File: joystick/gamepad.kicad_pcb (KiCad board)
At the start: 2 copper layers, 112 x 47.6 mm, 40 parts, among them IC1 ATTINY45-S, P2 CONN_01X04, SW1 SW_PUSH, SW2 SW_PUSH, SW3 SW_PUSH, SW4 SW_PUSH, SW5 SW_PUSH, SW6 SW_PUSH, U1 74LS165, U2 74164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

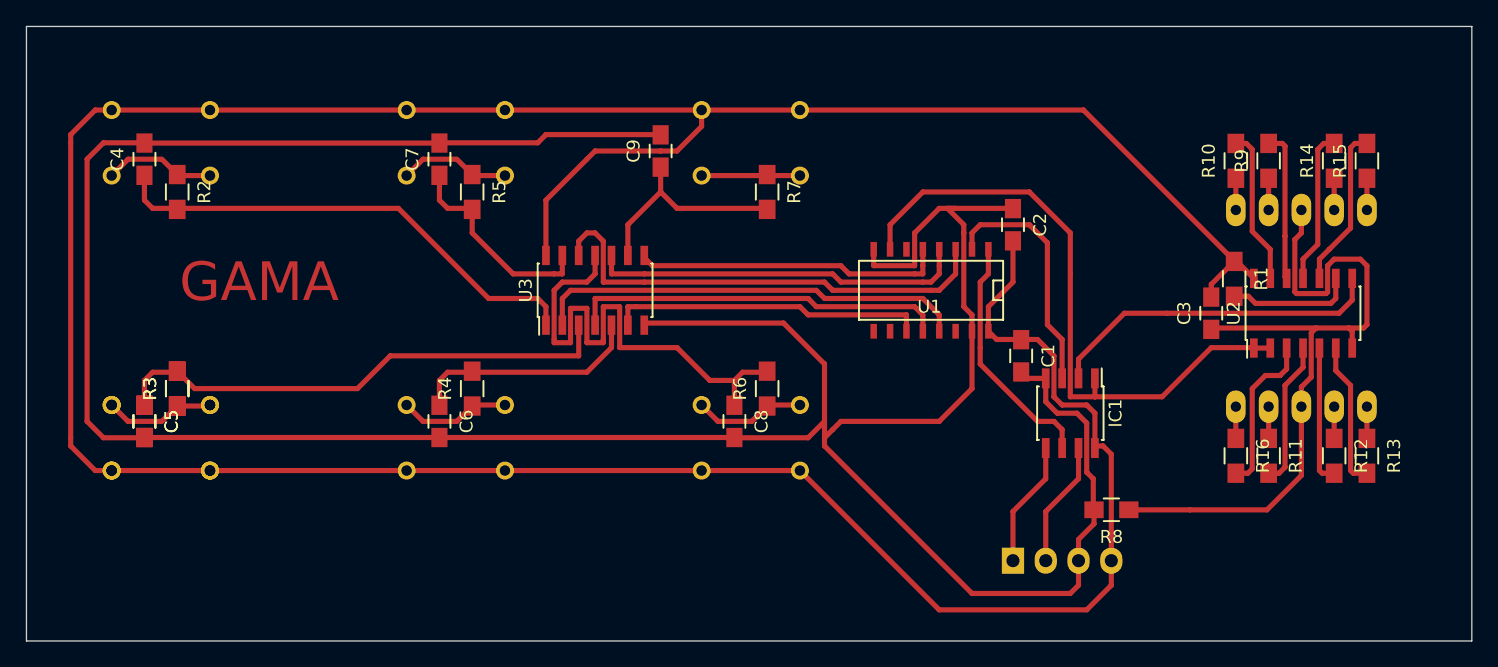
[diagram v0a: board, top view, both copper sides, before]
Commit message: Fixed hardware bug (74LS14 inputs were left floating) Changed schematics accordingly
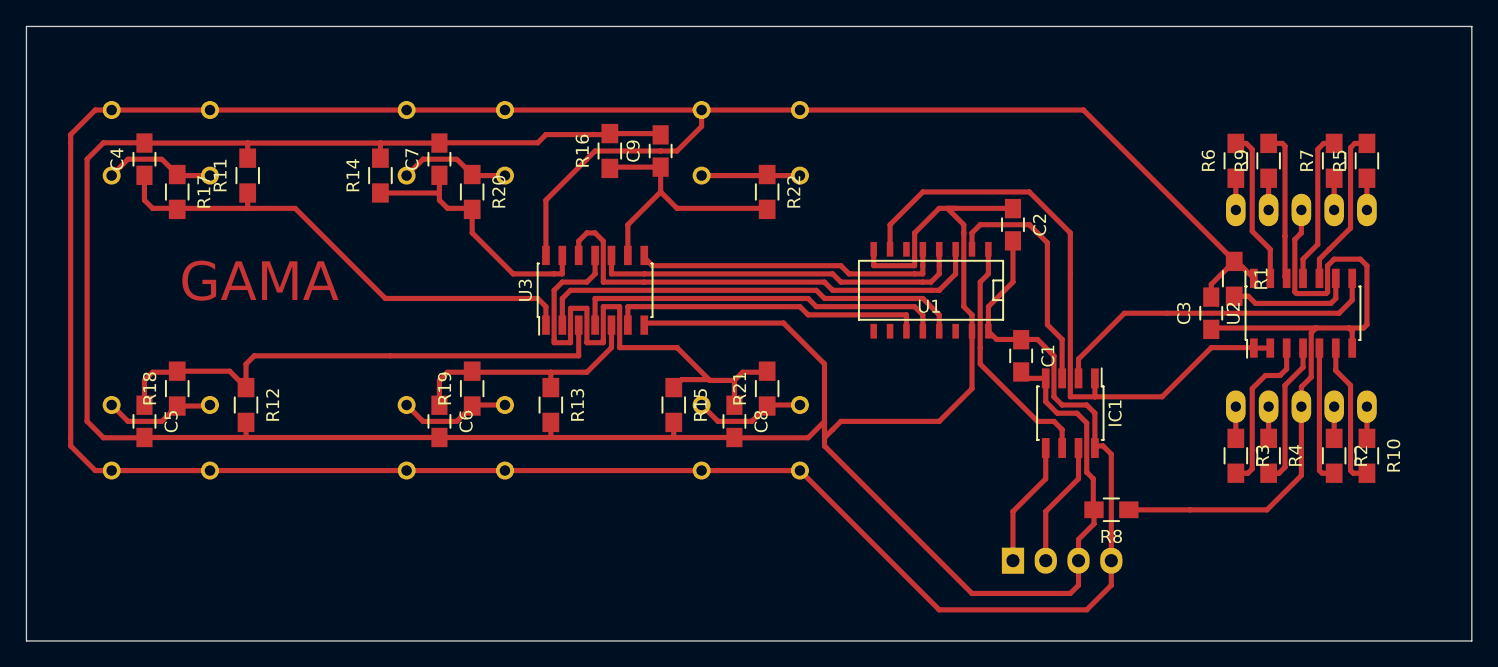
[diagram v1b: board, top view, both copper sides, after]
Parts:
- removed the C5 at (86.4, 120.7)
- removed the R3 at (88.9, 118.1)
- removed the SW2 at (87.6, 121.9)
- added R11: 1k, Resistors_SMD:R_0805_HandSoldering, F.Cu at (94.4, 101.6)
- added R12: 1k, Resistors_SMD:R_0805_HandSoldering, F.Cu at (94.2, 119.4)
- added R13: 1k, Resistors_SMD:R_0805_HandSoldering, F.Cu at (117.9, 119.4)
- added R14: 1k, Resistors_SMD:R_0805_HandSoldering, F.Cu at (104.6, 101.6)
- added R15: 1k, Resistors_SMD:R_0805_HandSoldering, F.Cu at (127.4, 119.4)
- added R16: 1k, Resistors_SMD:R_0805_HandSoldering, F.Cu at (122.4, 99.7)
- C1, C2, C3: value C -> 100nF
- C4, C5, C6, C7, C8, C9: value C -> 1uF
- R1: value R -> 10k
- R10: renamed from R13; value R -> 120
- R17: renamed from R2; value R -> 1k
- R18: renamed from R3; value R -> 1k
- R19: renamed from R4; value R -> 1k
- R2: renamed from R12; value R -> 120
- R20: renamed from R5; value R -> 1k
- R21: renamed from R6; value R -> 1k
- R22: renamed from R7; value R -> 1k
- R3: renamed from R16; value R -> 120
- R4: renamed from R11; value R -> 120
- R5: renamed from R15; value R -> 120
- R6: renamed from R10; value R -> 120
- R7: renamed from R14; value R -> 120
- R8: value R -> 0
- R9: value R -> 120
- renumbered P2 to P1
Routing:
- net GND: track 296.8 -> 302.8 mm
- net Net-(C7-Pad1): track 16.3 -> 21.1 mm
- net Net-(C9-Pad1): track 16.7 -> 20.7 mm
- net Net-(C8-Pad1): track 40.4 -> 43.4 mm
- net Net-(C6-Pad1): track 18.3 -> 19.5 mm
- net Net-(C4-Pad1): track 38.0 -> 39.1 mm
- net Net-(C5-Pad1): track 45.1 -> 46.1 mm
